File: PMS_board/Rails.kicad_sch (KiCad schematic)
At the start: 40 parts, among them J1 D1, J2 D2, J3 D3, J4 D4, J5 T1, J6 T2, J7 T3, J8 T4

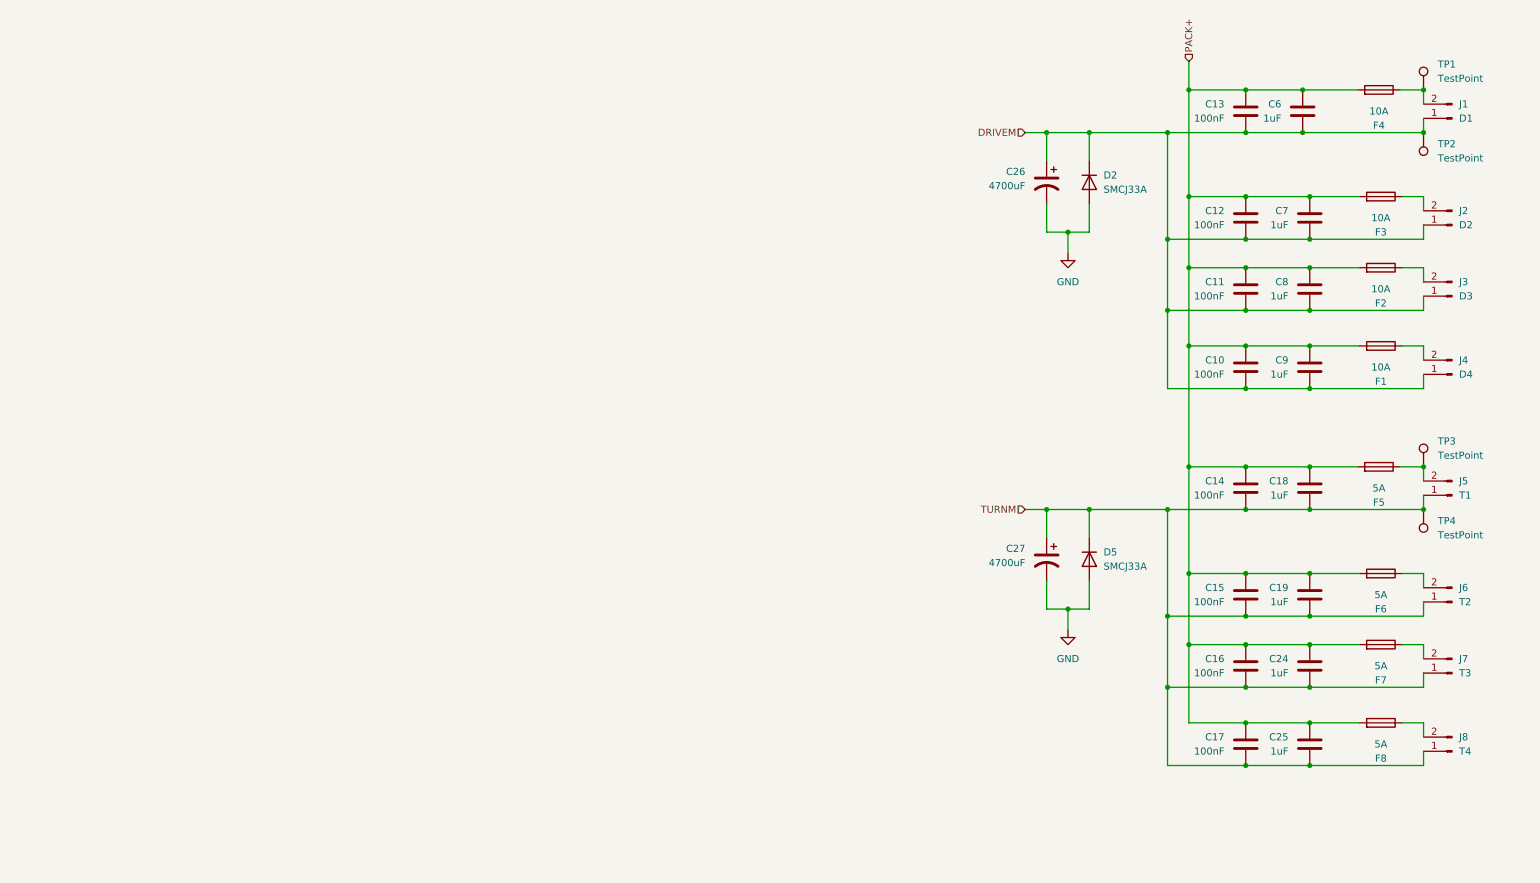
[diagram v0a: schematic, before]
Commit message: Finished preliminary load switching circuit
Except for the Aux
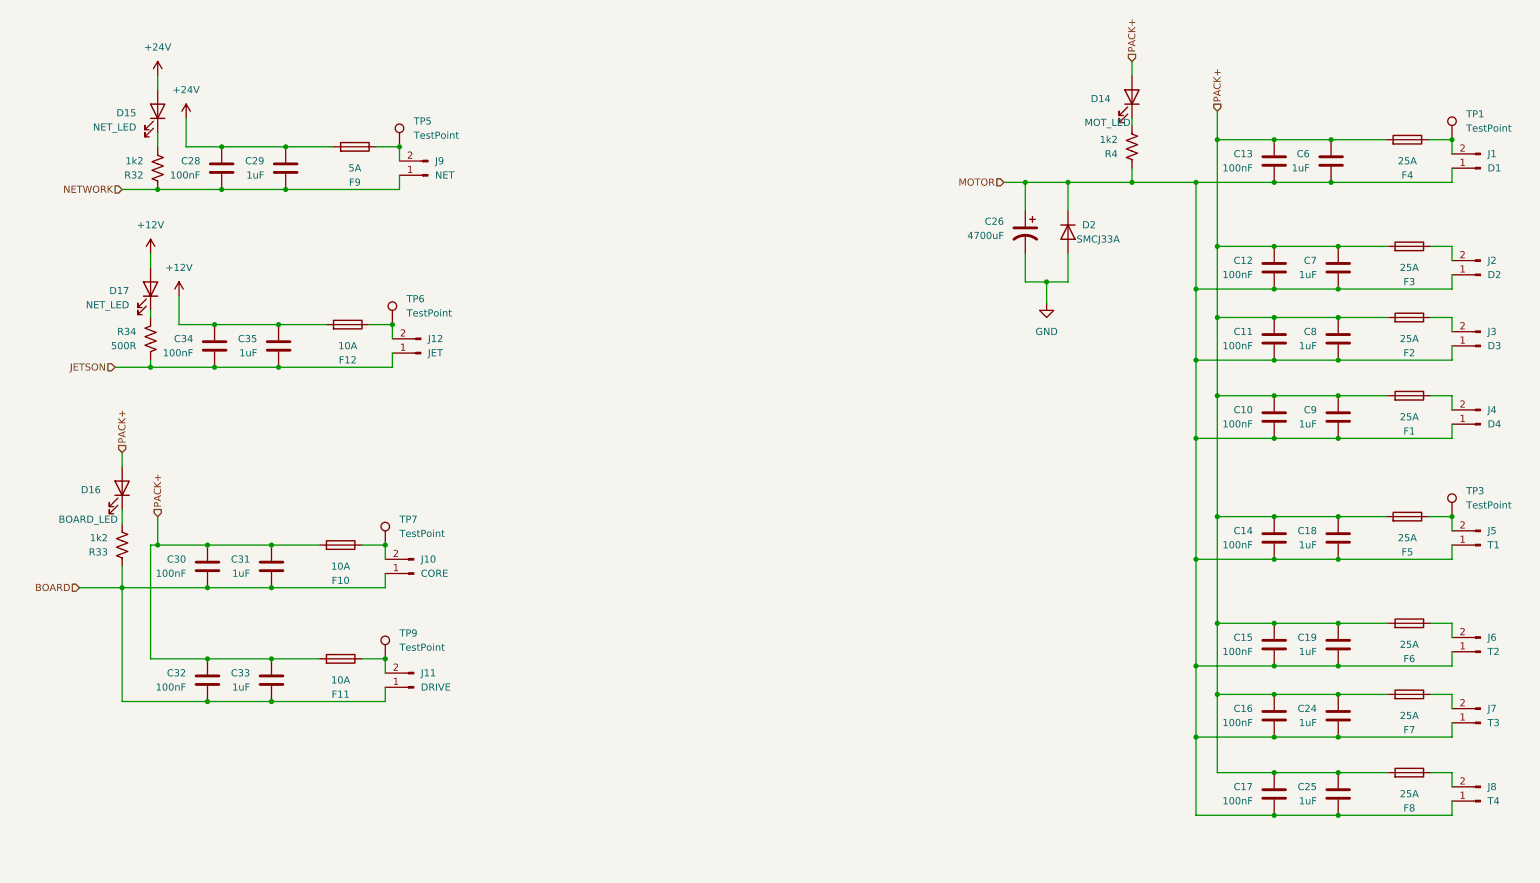
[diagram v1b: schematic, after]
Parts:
- removed C27: 4700uF, symbol Device:C_Polarized_US
- removed D5: SMCJ33A, symbol Device:D
- removed TP2, TP4: TestPoint, symbol Connector:TestPoint
- added C28, C30, C32, C34: 100nF, symbol Device:C
- added C29, C31, C33, C35: 1uF, symbol Device:C
- added D14: MOT_LED, LED_SMD:LED_Cree-XHP50_3V_HighDensity, symbol Device:LED
- added D15, D17: NET_LED, symbol Device:LED
- added D16: BOARD_LED, symbol Device:LED
- added F10, F11, F12: 10A, Package_LCC:PLCC-84_29.3x29.3mm_P1.27mm, symbol Device:Fuse
- added F9: 5A, Package_LCC:PLCC-84_29.3x29.3mm_P1.27mm, symbol Device:Fuse
- added J10: CORE, Connector:Tag-Connect_TC2030-IDC-FP_2x03_P1.27mm_Vertical, symbol Connector:Conn_01x02_Pin
- added J11: DRIVE, Connector:Tag-Connect_TC2030-IDC-FP_2x03_P1.27mm_Vertical, symbol Connector:Conn_01x02_Pin
- added J12: JET, Connector:Tag-Connect_TC2030-IDC-FP_2x03_P1.27mm_Vertical, symbol Connector:Conn_01x02_Pin
- added J9: NET, Connector:Tag-Connect_TC2030-IDC-FP_2x03_P1.27mm_Vertical, symbol Connector:Conn_01x02_Pin
- added R32, R33, R4: 1k2, symbol Device:R_US
- added R34: 500R, symbol Device:R_US
- added TP5, TP6, TP7, TP9: TestPoint, Relay_THT:Relay_DPDT_Schrack-RT2-FormC_RM5mm, symbol Connector:TestPoint
- F1, F2, F3, F4: value 10A -> 25A
- F5, F6, F7, F8: value 5A -> 25A
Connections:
- net TURNM is gone; now on net MOTOR: C14.2, C15.2, C16.2, C17.2, C18.2, C19.2, C24.2, C25.2, J5.1 (Pin_1), J6.1 (Pin_1), J7.1 (Pin_1), J8.1 (Pin_1)
- net PACK+: now also C30.1, C31.1, C32.1, C33.1, D14.2 (A), D16.2 (A), F10.2, F11.2
- net DRIVEM renamed MOTOR
- net MOTOR: now also R4.1
- new net: D14.1 (K), R4.2
- new net: F10.1, J10.2 (Pin_2), TP7.1
- new net: D15.1 (K), R32.2
- new net: F9.1, J9.2 (Pin_2), TP5.1
- new net: F11.1, J11.2 (Pin_2), TP9.1
- new net: D16.1 (K), R33.2
- new net: F12.1, J12.2 (Pin_2), TP6.1
- new net: D17.1 (K), R34.2
- new net +12V: C34.1, C35.1, D17.2 (A), F12.2
- new net +24V: C28.1, C29.1, D15.2 (A), F9.2
- new net BOARD: C30.2, C31.2, C32.2, C33.2, J10.1 (Pin_1), J11.1 (Pin_1), R33.1
- new net JETSON: C34.2, C35.2, J12.1 (Pin_1), R34.1
- new net NETWORK: C28.2, C29.2, J9.1 (Pin_1), R32.1
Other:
- moved on the sheet: C10, C11, C12, C13, C14, C15, C16, C17, C18, C19, C24, C25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

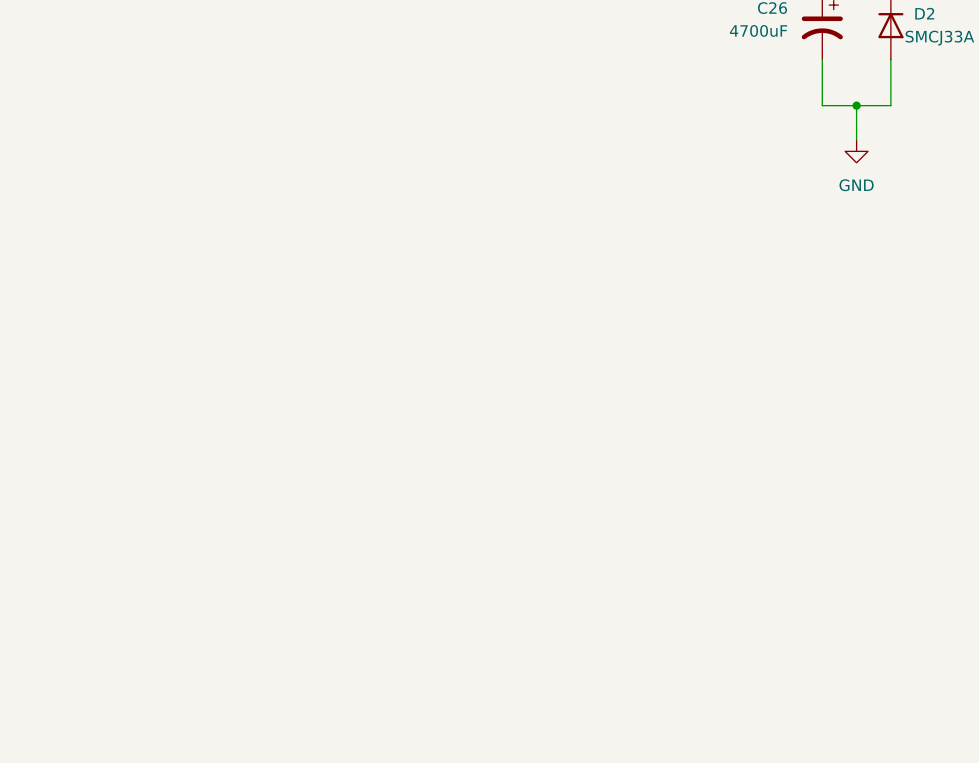
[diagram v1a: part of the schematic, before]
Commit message: Added Aux rail
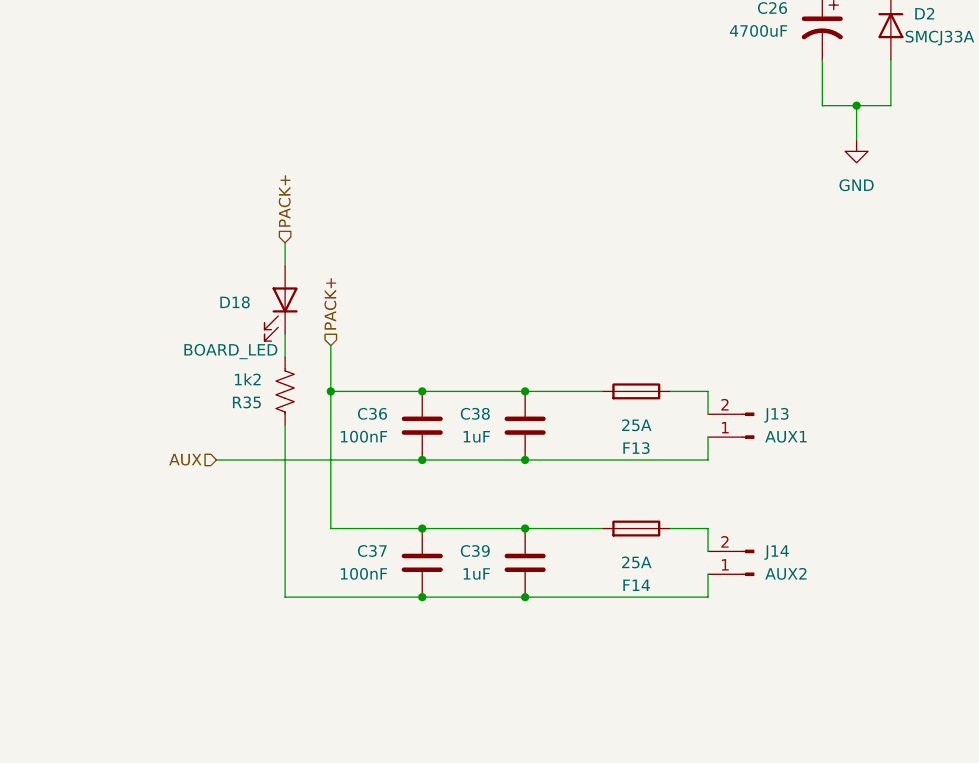
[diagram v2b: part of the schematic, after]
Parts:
- added C36, C37: 100nF, symbol Device:C
- added C38, C39: 1uF, symbol Device:C
- added D18: BOARD_LED, symbol Device:LED
- added F13, F14: 25A, Package_LCC:PLCC-84_29.3x29.3mm_P1.27mm, symbol Device:Fuse
- added J13: AUX1, Connector:Tag-Connect_TC2030-IDC-FP_2x03_P1.27mm_Vertical, symbol Connector:Conn_01x02_Pin
- added J14: AUX2, Connector:Tag-Connect_TC2030-IDC-FP_2x03_P1.27mm_Vertical, symbol Connector:Conn_01x02_Pin
- added R35: 1k2, symbol Device:R_US
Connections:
- net PACK+: now also C36.1, C37.1, C38.1, C39.1, D18.2 (A), F13.2, F14.2
- new net: C37.2, C39.2, J14.1 (Pin_1), R35.1
- new net: D18.1 (K), R35.2
- new net: F14.1, J14.2 (Pin_2)
- new net: F13.1, J13.2 (Pin_2)
- new net AUX: C36.2, C38.2, J13.1 (Pin_1)

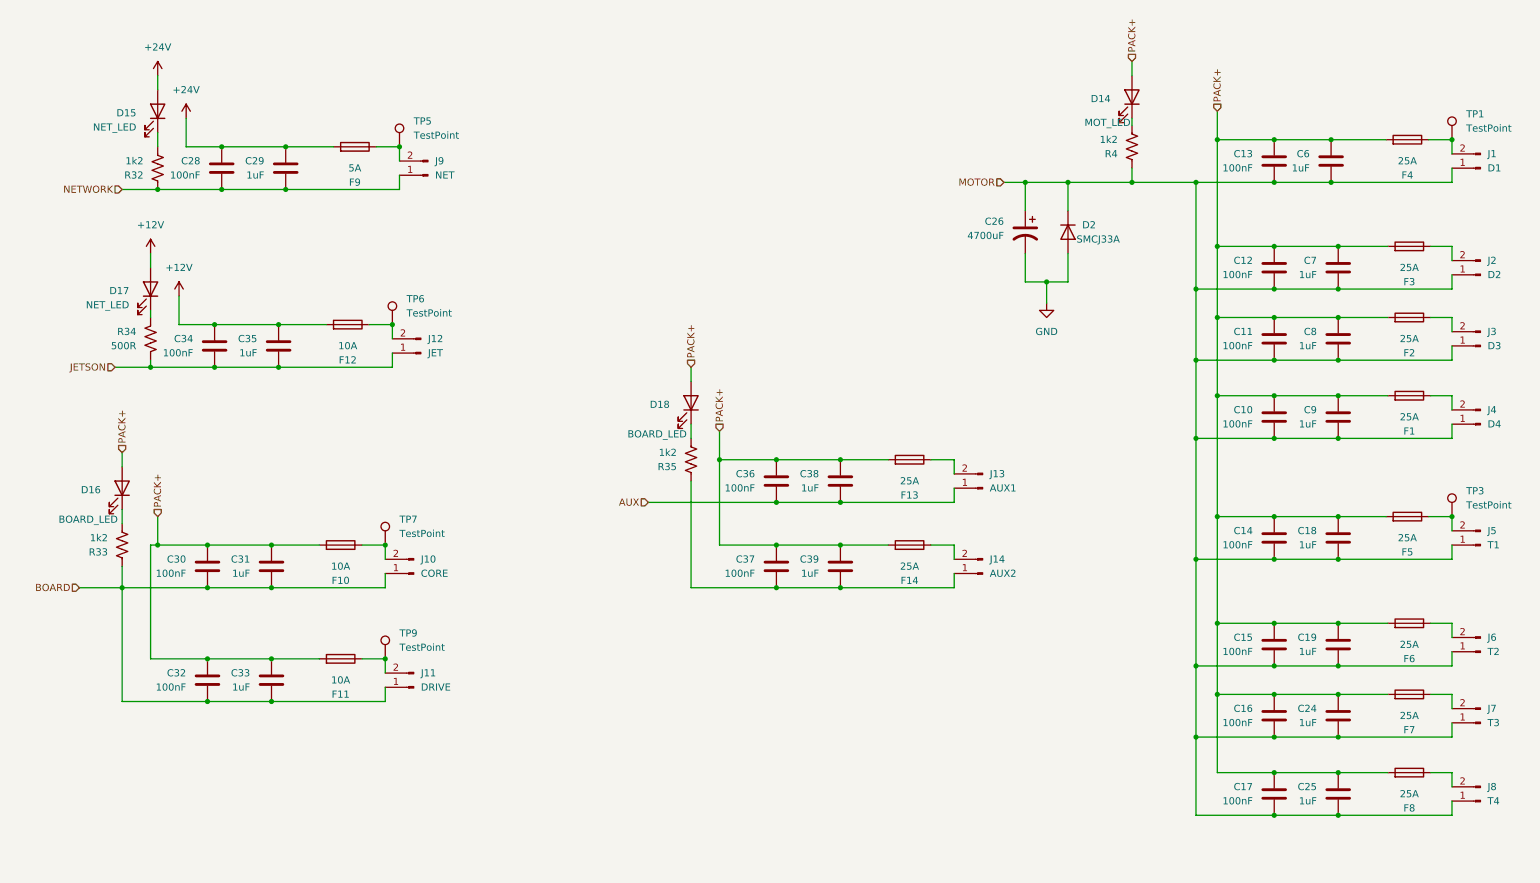
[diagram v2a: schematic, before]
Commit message: Cleaned up Output Sheet
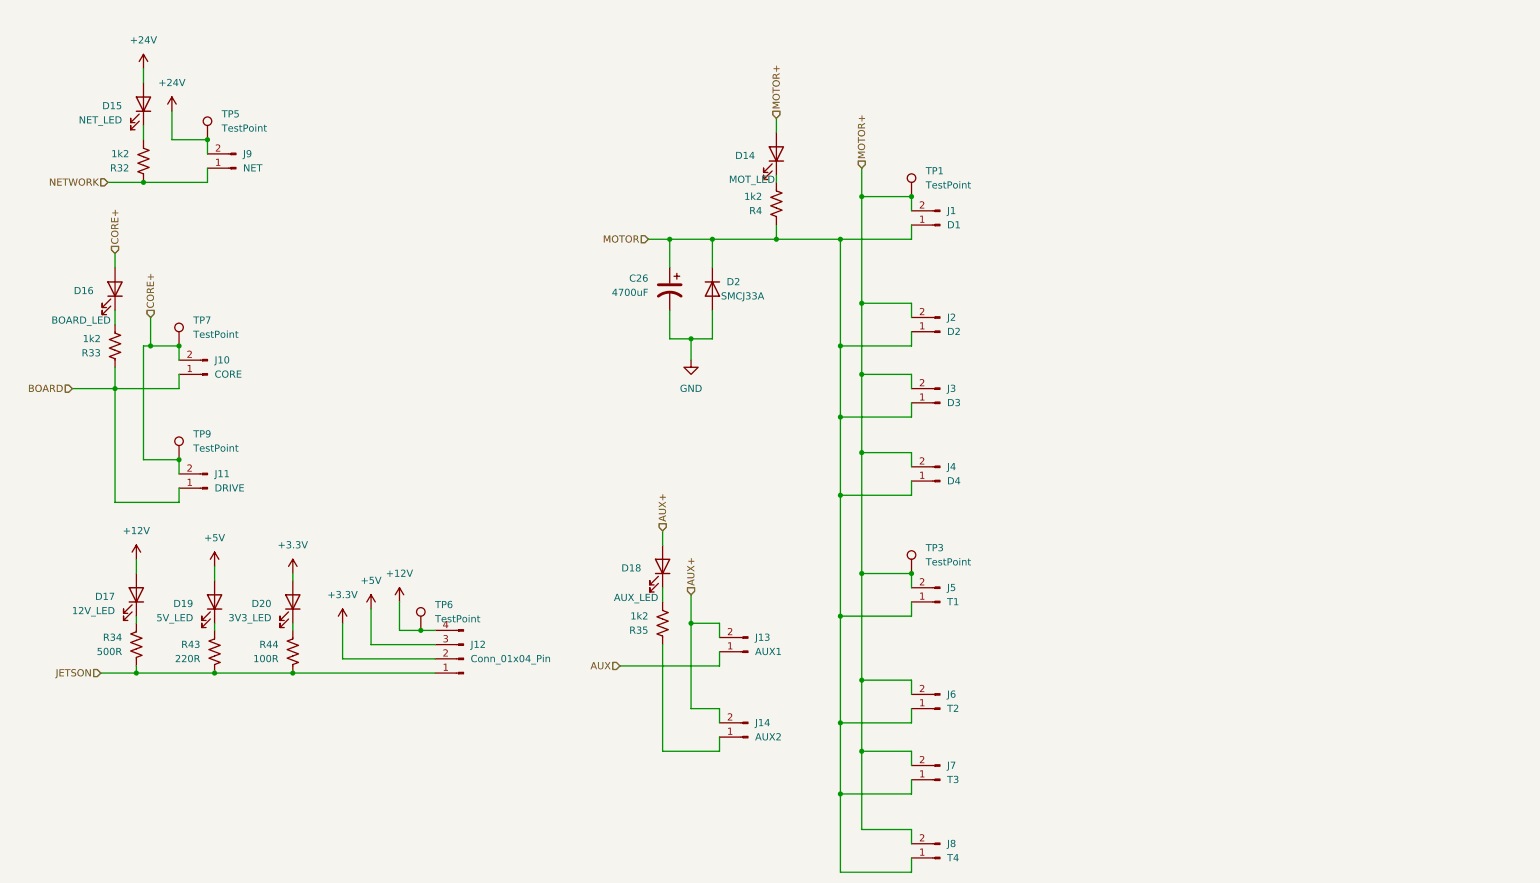
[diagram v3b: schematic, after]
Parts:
- removed C10, C11, C12, C13, C14, C15, C16, C17, C28, C30, C32, C34, C36, C37: 100nF, symbol Device:C
- removed C18, C19, C24, C25, C29, C31, C33, C35, C38, C39, C6, C7, C8, C9: 1uF, symbol Device:C
- removed F1, F13, F14, F2, F3, F4, F5, F6, F7, F8: 25A, Package_LCC:PLCC-84_29.3x29.3mm_P1.27mm, symbol Device:Fuse
- removed F10, F11, F12: 10A, Package_LCC:PLCC-84_29.3x29.3mm_P1.27mm, symbol Device:Fuse
- removed F9: 5A, Package_LCC:PLCC-84_29.3x29.3mm_P1.27mm, symbol Device:Fuse
- removed J12: JET, Connector:Tag-Connect_TC2030-IDC-FP_2x03_P1.27mm_Vertical, symbol Connector:Conn_01x02_Pin
- added D19: 5V_LED, symbol Device:LED
- added D20: 3V3_LED, symbol Device:LED
- added J12: Conn_01x04_Pin, symbol Connector:Conn_01x04_Pin
- added R43: 220R, symbol Device:R_US
- added R44: 100R, symbol Device:R_US
- D17: value NET_LED -> 12V_LED
- D18: value BOARD_LED -> AUX_LED
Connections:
- net +12V: now also TP6.1, J12.4 (Pin_4)
- net +24V: now also J9.2 (Pin_2), TP5.1
- net JETSON: now also J12.1 (Pin_1), R43.1, R44.1
- net CORE+: now reaches J10.2 (Pin_2), TP7.1
- net CORE+: now also D16.2 (A), J11.2 (Pin_2), TP9.1
- net MOTOR+: now reaches J8.2 (Pin_2)
- net MOTOR+: now also D14.2 (A), J1.2 (Pin_2), J2.2 (Pin_2), J3.2 (Pin_2), J4.2 (Pin_2), J5.2 (Pin_2), J6.2 (Pin_2), J7.2 (Pin_2), TP1.1, TP3.1
- net AUX+: now reaches J14.2 (Pin_2)
- net AUX+: now also D18.2 (A), J13.2 (Pin_2)
- removed net PACK+: D14.2 (A), D16.2 (A), D18.2 (A)
- new net: D19.1 (K), R43.2
- new net: D20.1 (K), R44.2
- new net +3.3V: D20.2 (A), J12.2 (Pin_2)
- new net +5V: D19.2 (A), J12.3 (Pin_3)
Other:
- moved on the sheet: C26, D14, D15, D16, D17, D18, D2, J1, J10, J11, J13, J14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

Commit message: Swapped 3.3V in jeteson output rail with 3.3V (Jetson)
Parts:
- J12: value Conn_01x04_Pin -> JETSON
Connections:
- net +3.3V: no longer D20.2 (A)
- new net +3V3 (Jetson): D20.2 (A)
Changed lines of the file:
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@@
-	)
-	(symbol
-		(lib_id "power:+3.3V")
-		(at 60.96 111.76 0)
-		(unit 1)
-		(body_style 1)
-		(exclude_from_sim no)
-		(in_bom yes)
-		(on_board yes)
-		(in_pos_files yes)
-		(dnp no)
-		(fields_autoplaced yes)
-		(property "Reference" "#PWR070"
-			(at 60.96 115.57 0)
-			(hide yes)
-			(show_name no)
-			(do_not_autoplace no)
-			(effects
-				(font
-					(size 1.27 1.27)
-				)
-			)
-		)
-		(property "Value" "+3.3V"
-			(at 60.96 106.68 0)
-			(show_name no)
-			(do_not_autoplace no)
-			(effects
-				(font
-					(size 1.27 1.27)
-				)
-			)
-		)
-		(property "Footprint" ""
-			(at 60.96 111.76 0)
-			(hide yes)
-			(show_name no)
-			(do_not_autoplace no)
-			(effects
-				(font
-					(size 1.27 1.27)
-				)
-			)
-		)
-		(property "Datasheet" ""
-			(at 60.96 111.76 0)
-			(hide yes)
-			(show_name no)
-			(do_not_autoplace no)
-			(effects
-				(font
-					(size 1.27 1.27)
-				)
-			)
-		)
-		(property "Description" "Power symbol creates a global label with name \"+3.3V\""
-			(at 60.96 111.76 0)
-			(hide yes)
-			(show_name no)
-			(do_not_autoplace no)
-			(effects
-				(font
-					(size 1.27 1.27)
-				)
-			)
-		)
-		(pin "1"
-		)
-		(instances
-			(project "PMS_board"
-				(path "/282246b0-e0d8-4997-b3ee-58bf10355d52/266cb597-81f7-4ea7-87c1-e1b826fc674e/1ce466be-8c1f-42c9-b575-af9917f46ea9"
-					(reference "#PWR070")
-					(unit 1)
-				)
-			)
-		)
 	)
 	(symbol
@@
 	)
 	(symbol
+		(lib_id "power:+3V3")
+		(at 60.96 111.76 0)
+		(unit 1)
+		(body_style 1)
+		(exclude_from_sim no)
+		(in_bom yes)
+		(on_board yes)
+		(in_pos_files yes)
+		(dnp no)
+		(fields_autoplaced yes)
+		(property "Reference" "#PWR069"
+			(at 60.96 115.57 0)
+			(hide yes)
+			(show_name no)
+			(do_not_autoplace no)
+			(effects
+				(font
+					(size 1.27 1.27)
+				)
+			)
+		)
+		(property "Value" "+3V3 (Jetson)"
+			(at 60.96 106.68 0)
+			(show_name no)
+			(do_not_autoplace no)
+			(effects
+				(font
+					(size 1.27 1.27)
+				)
+			)
+		)
+		(property "Footprint" ""
+			(at 60.96 111.76 0)
+			(hide yes)
+			(show_name no)
+			(do_not_autoplace no)
+			(effects
+				(font
+					(size 1.27 1.27)
+				)
+			)
+		)
+		(property "Datasheet" ""
+			(at 60.96 111.76 0)
+			(hide yes)
+			(show_name no)
+			(do_not_autoplace no)
+			(effects
+				(font
+					(size 1.27 1.27)
+				)
+			)
+		)
+		(property "Description" "Power symbol creates a global label with name \"+3V3\""
+			(at 60.96 111.76 0)
+			(hide yes)
+			(show_name no)
+			(do_not_autoplace no)
+			(effects
+				(font
+					(size 1.27 1.27)
+				)
+			)
+		)
+		(pin "1"
+		)
+		(instances
+			(project "PMS_board"
+				(path "/282246b0-e0d8-4997-b3ee-58bf10355d52/266cb597-81f7-4ea7-87c1-e1b826fc674e/1ce466be-8c1f-42c9-b575-af9917f46ea9"
+					(reference "#PWR069")
+					(unit 1)
+				)
+			)
+		)
+	)
+	(symbol
 		(lib_id "Connector:Conn_01x02_Pin")
 		(at 176.53 68.58 180)
@@
 			)
 		)
-		(property "Value" "Conn_01x04_Pin"
+		(property "Value" "JETSON"
 			(at 92.71 126.9999 0)
 			(show_name no)
